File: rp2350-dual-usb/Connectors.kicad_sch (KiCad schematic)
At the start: 17 parts, among them J2 USB_C_Receptacle_USB2.0_16P, J3 USB_C_Receptacle_USB2.0_14P, J4 TRS, J5 TRS, U3 USBLC6-2SC6, U4 USBLC6-2SC6, U5 HCPL-0631

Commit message: Updates YouMe Transformer to v1.1, fixing incorrect R10 value. Improves the consistency of the Lichen symbol library.
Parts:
- R10: value 7k7_0603 -> 4.7K; Display 4.7k -> 4K7; Specifications 4k7, 1%, 1/10W, 0603 -> (none)
- R11: value 33R_0402 -> 33R
- R12: value 10R_0402 -> 10R
- R13, R14: value 220R_0402 -> 220R
- R15: value 470R_0402 -> 470R
- R7, R8: value 5k1_0603 -> 5.1K; Display 5.1K -> 5K1
- R9: value 4k7_0603 -> 4.7K; Display 4.7k -> 4K7; Specifications 4k7, 1%, 1/10W, 0603 -> (none)
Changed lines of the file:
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@@
 			)
 		)
-		(property "Value" "470R_0402"
+		(property "Value" "470R"
 			(at 223.52 101.6 90)
 			(effects
@@
 			)
 		)
-		(property "Value" "220R_0402"
+		(property "Value" "220R"
 			(at 201.93 105.41 90)
 			(effects
@@
 			)
 		)
-		(property "Value" "5k1_0603"
+		(property "Value" "5.1K"
 			(at 73.66 60.96 90)
 			(effects
@@
 			)
 		)
-		(property "Display" "5.1K"
+		(property "Display" "5K1"
 			(at 73.66 54.61 90)
 			(effects
@@
 			)
 		)
-		(property "Value" "7k7_0603"
+		(property "Value" "4.7K"
 			(at 76.2 115.57 90)
 			(effects
@@
 			)
 		)
-		(property "Display" "4.7k"
+		(property "Display" "4K7"
 			(at 76.2 121.92 90)
 			(effects
@@
 					(size 1.27 1.27)
 				)
-			)
-		)
-		(property "Specifications" "4k7, 1%, 1/10W, 0603"
-			(at 68.326 115.57 0)
-			(effects
-				(font
-					(size 1.27 1.27)
-				)
-				(justify left)
-				(hide yes)
 			)
 		)
@@
 			)
 		)
-		(property "Value" "220R_0402"
+		(property "Value" "220R"
 			(at 201.93 115.57 90)
 			(effects
@@
 			)
 		)
-		(property "Value" "5k1_0603"
+		(property "Value" "5.1K"
 			(at 73.66 58.42 90)
 			(effects
@@
 			)
 		)
-		(property "Display" "5.1K"
+		(property "Display" "5K1"
 			(at 73.66 64.77 90)
 			(effects
@@
 			)
 		)
-		(property "Value" "4k7_0603"
+		(property "Value" "4.7K"
 			(at 76.2 118.11 90)
 			(effects
@@
 			)
 		)
-		(property "Display" "4.7k"
+		(property "Display" "4K7"
 			(at 76.2 111.76 90)
 			(effects
@@
 					(size 1.27 1.27)
 				)
-			)
-		)
-		(property "Specifications" "4k7, 1%, 1/10W, 0603"
-			(at 68.326 118.11 0)
-			(effects
-				(font
-					(size 1.27 1.27)
-				)
-				(justify left)
-				(hide yes)
 			)
 		)
@@
 			)
 		)
-		(property "Value" "10R_0402"
+		(property "Value" "10R"
 			(at 201.93 64.77 90)
 			(effects
@@
 			)
 		)
-		(property "Value" "33R_0402"
+		(property "Value" "33R"
 			(at 201.93 67.31 90)
 			(effects

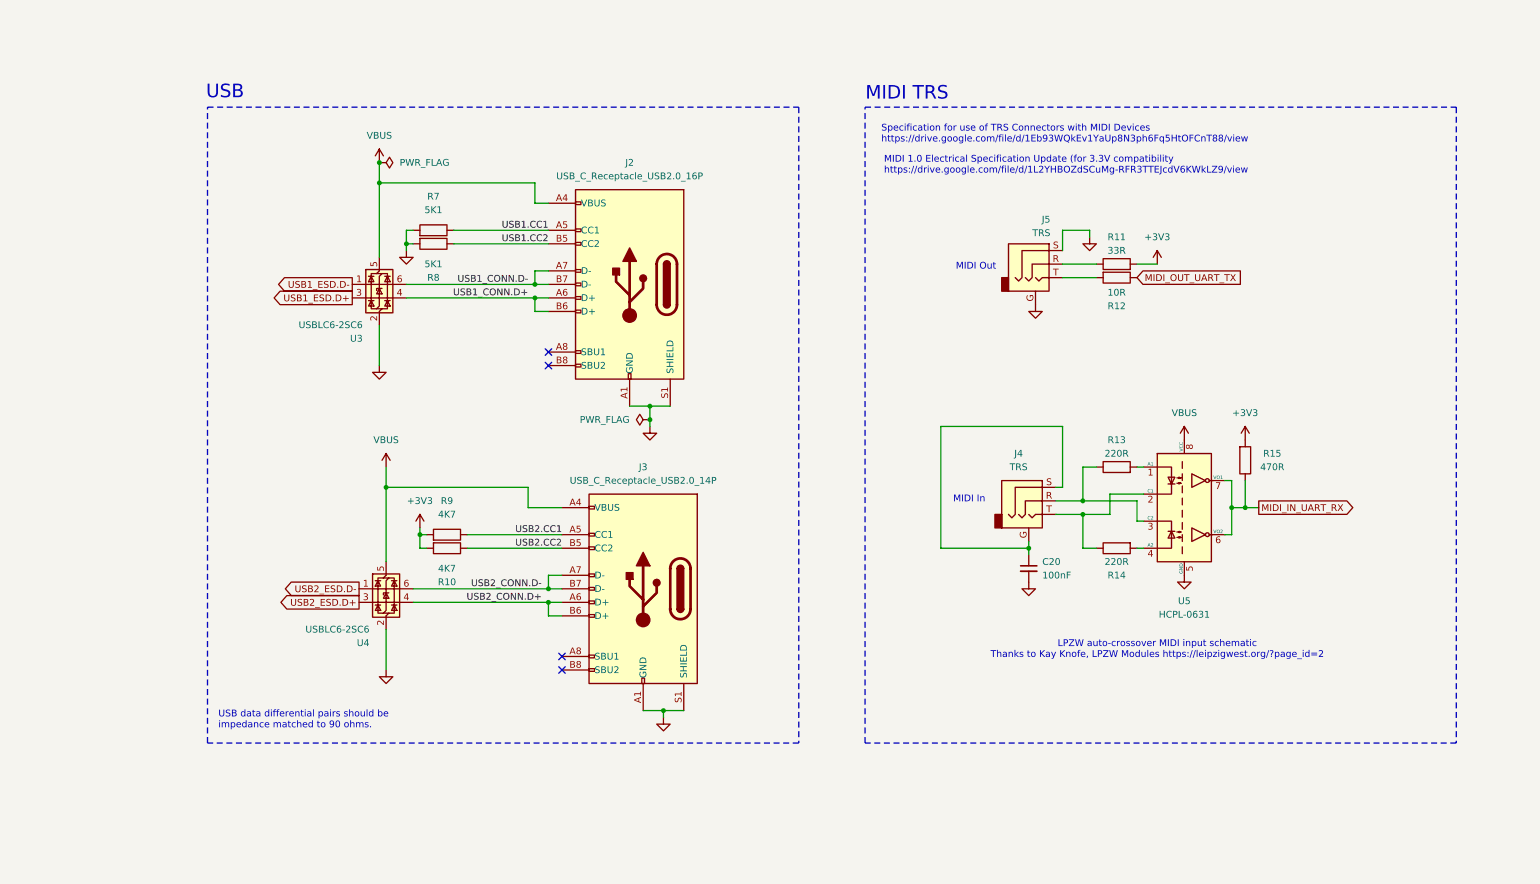
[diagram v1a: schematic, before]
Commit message: feat: Updates symbol libraries and design blocks. Adds in-progress RP2350-based module.
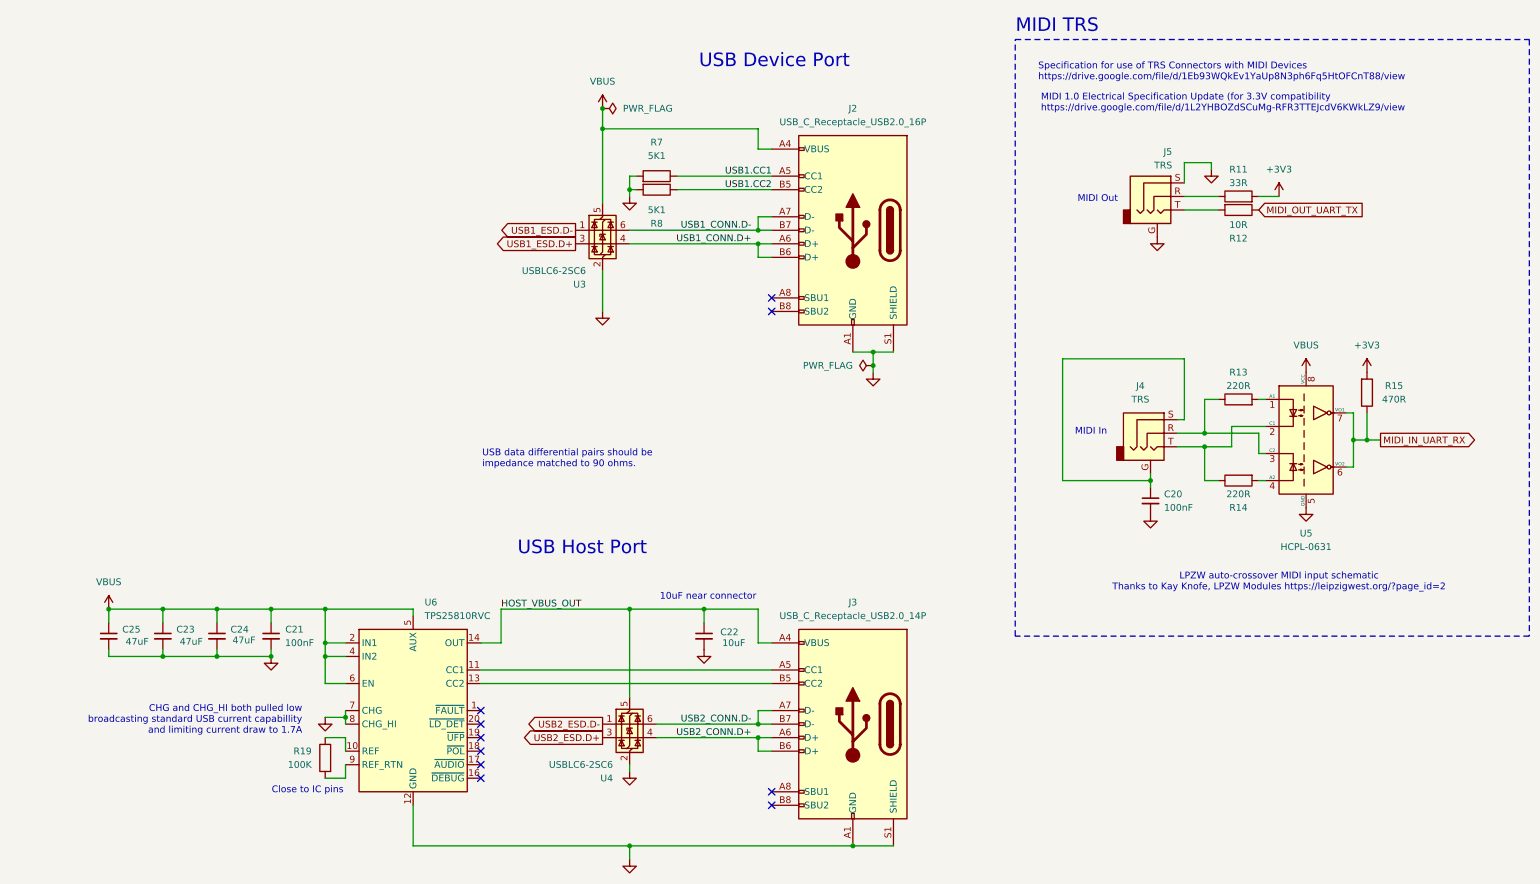
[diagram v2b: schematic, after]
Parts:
- removed R10, R9: 4.7K, Lichen:R_0603, symbol Lichen:4.7k_0603
- added C21: 100nF, Lichen:C_0603, symbol Lichen:100nF_0603_50V
- added C22: 10uF, Lichen:C_0603, symbol Lichen:10uF_0603_25V
- added C23, C24, C25: 47uF, Capacitor_SMD:C_1206_3216Metric, symbol Lichen:100nF_C0G_1206_50V
- added R19: 100K, Lichen:R_0402_1005Metric, symbol Lichen:100K_0402
- added U6: TPS25810RVC, Lichen:Texas_RVC0020A_WQFN-20-1EP_3x4mm_P0.5mm_EP1.6x2.6mm_ThermalVias, symbol Lichen:TPS25810RVC
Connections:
- net GND: now also C21.2, C22.2, C23.2, C24.2, C25.2, U6.12 (GND), U6.21 (GND), U6.7 (CHG), U6.8 (CHG_HI)
- net VBUS: now also C21.1, C23.1, C24.1, C25.1, U6.2 (IN1), U6.3 (IN1), U6.4 (IN2), U6.5 (AUX), U6.6 (EN); no longer J3.A4 (VBUS), J3.A9 (VBUS), J3.B4 (VBUS), J3.B9 (VBUS), U4.5 (VBUS)
- net USB2.CC1: no longer names the net of J3.A5 (CC1)
- net USB2.CC1: now also U6.11 (CC1)
- net USB2.CC2: no longer names the net of J3.B5 (CC2)
- net USB2.CC2: now also U6.13 (CC2)
- new net: R19.1, U6.10 (REF)
- new net: R19.2, U6.9 (REF_RTN)
- new net HOST_VBUS_OUT: C22.1, J3.A4 (VBUS), J3.A9 (VBUS), J3.B4 (VBUS), J3.B9 (VBUS), U4.5 (VBUS), U6.14 (OUT), U6.15 (OUT)
- no-connect marks 4 -> 10
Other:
- note added: "10uF near connector"
- note added: "CHG and CHG_HI both pulled low broadcasting standard USB current capabillity and limiting current draw to 1.7A"
- note added: "Close to IC pins"
- note added: "USB Device Port"
- note added: "USB Host Port"
- note removed: "USB"
- moved on the sheet: C20, J2, J3, J4, J5, R11, R12, R13, R14, R15, R7, R8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
